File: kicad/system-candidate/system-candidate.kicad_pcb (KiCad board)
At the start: 4 copper layers, 153 x 79.1 mm, 76 parts, among them J1 691137710002 2P 5.00mm, J2 Auxiliary 12V, J3 Differential audio, J4 Control 2x4: 3V3 RESET FAULT 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, J5 691137710002 2P 5.00mm, J6 GND braid solder bond - NO mo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, U1 TPA3255DDV, U2 OPA1656ID, U3 OPA1656ID

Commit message: feat(eda): capture discrete D-020 sequencer and integrate D-021 power into system candidate
- seq-d020 (D-023): LP2985 3.3 V, two TPS3808 stages (>=360 ms hold),
  74LVC2G74 RUN/ARMED latches (human start edge with CLIP_OTW high, FAULT
  arming and latch with human re-arm), 0.62-1.44 s start timeout, TPS3700
  windows for ANALOG_12V and VMID on the RAILS_OK wired-AND.
- seq_d020_logic simulates the captured netlist; mutation-checked tests.
- system-candidate: power and seq banks outside the OEM outline, 150
  footprints, 421 native pins matched; PVDD_36V renamed PVDD; J4/R7/R8 DNP.
  ERC equal to base (4 PBTL OUT_x, 1 MONO_BIASED), DRC 0, 338 unrouted.
- power-d021: candidate stock footprints, SEQ_3V3 pull-up, manifest restored.
- 3D gallery adds system candidate views framed to show import banks.
- D-019 isolation, discharge, DC sense and mute remain NOT implemented.
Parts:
- added C301: 4700u 63V, Capacitor_THT:CP_Radial_D25.0mm_P10.00mm_SnapIn, F.Cu at (350.0, 130.0)
- added C302: 4700u 63V, Capacitor_THT:CP_Radial_D25.0mm_P10.00mm_SnapIn, F.Cu at (390.0, 130.0)
- added C310: 2.2u 100V X7R, Capacitor_SMD:C_1210_3225Metric, F.Cu at (310.0, 162.0)
- added C311: 2.2u 100V X7R, Capacitor_SMD:C_1210_3225Metric, F.Cu at (350.0, 162.0)
- added C312: 2.2n 50V X7R, Capacitor_SMD:C_0402_1005Metric, F.Cu at (390.0, 162.0)
- added C313: 3.3n, Capacitor_SMD:C_0603_1608Metric, F.Cu at (390.0, 194.0)
- added C314: 56p, Capacitor_SMD:C_0603_1608Metric, F.Cu at (190.0, 226.0)
- added C315: 22u 25V X7R, Capacitor_SMD:C_1210_3225Metric, F.Cu at (230.0, 226.0)
- added C316: 22u 25V X7R, Capacitor_SMD:C_1210_3225Metric, F.Cu at (270.0, 226.0)
- added C320: 100n, Capacitor_SMD:C_0603_1608Metric, F.Cu at (230.0, 258.0)
- added C401: 1u 25V, Capacitor_SMD:C_0603_1608Metric, F.Cu at (412.0, 25.0)
- added C402: 10n, Capacitor_SMD:C_0603_1608Metric, F.Cu at (434.0, 25.0)
- added C403: 2.2u 10V, Capacitor_SMD:C_0603_1608Metric, F.Cu at (456.0, 25.0)
- added C404: 180n, Capacitor_SMD:C_0603_1608Metric, F.Cu at (456.0, 43.0)
- added C405: 1u, Capacitor_SMD:C_0603_1608Metric, F.Cu at (390.0, 61.0)
- added C406: 100n, Capacitor_SMD:C_0603_1608Metric, F.Cu at (412.0, 79.0)
- added C407: 100n, Capacitor_SMD:C_0603_1608Metric, F.Cu at (434.0, 79.0)
- added C408: 100n, Capacitor_SMD:C_0603_1608Metric, F.Cu at (456.0, 79.0)
- added C409: 100n, Capacitor_SMD:C_0603_1608Metric, F.Cu at (478.0, 79.0)
- added C410: 100n, Capacitor_SMD:C_0603_1608Metric, F.Cu at (500.0, 79.0)
- added C411: 100n, Capacitor_SMD:C_0603_1608Metric, F.Cu at (522.0, 79.0)
- added C412: 100n, Capacitor_SMD:C_0603_1608Metric, F.Cu at (544.0, 79.0)
- added C413: 100n, Capacitor_SMD:C_0603_1608Metric, F.Cu at (390.0, 97.0)
- added C414: 100n, Capacitor_SMD:C_0603_1608Metric, F.Cu at (412.0, 97.0)
- added C415: 100n, Capacitor_SMD:C_0603_1608Metric, F.Cu at (434.0, 97.0)
- added C416: 100n, Capacitor_SMD:C_0603_1608Metric, F.Cu at (500.0, 115.0)
- added C417: 100n, Capacitor_SMD:C_0603_1608Metric, F.Cu at (522.0, 115.0)
- added D301: RECT >=400V, Diode_THT:D_P600_R-6_P12.70mm_Horizontal, F.Cu at (270.0, 130.0)
- added D302: RECT >=400V, Diode_THT:D_P600_R-6_P12.70mm_Horizontal, F.Cu at (310.0, 130.0)
- added D303: TVS VWM>=51V, Diode_SMD:D_SMC, F.Cu at (230.0, 162.0)
- added F301: T8A slow, Fuse:Fuseholder_Cylinder-5x20mm_Schurter_0031_8201_Horizontal_Open, F.Cu at (230.0, 130.0)
- added J301: T1_SECONDARY, Connector_JST:JST_VH_B3P-VH_1x03_P3.96mm_Vertical, F.Cu at (190.0, 130.0)
- added J401: START_BUTTON, Connector_PinHeader_2.54mm:PinHeader_1x02_P2.54mm_Vertical, F.Cu at (500.0, 43.0)
- added L301: 68u, Inductor_SMD:L_Coilcraft_MSS1246T-XXX, F.Cu at (190.0, 194.0)
- added R301: 4.7k 2W, Resistor_THT:R_Axial_DIN0414_L11.9mm_D4.5mm_P15.24mm_Horizontal, F.Cu at (190.0, 162.0)
- added R310: 100k 1%, Resistor_SMD:R_0603_1608Metric, F.Cu at (230.0, 194.0)
- added R311: 453k 1%, Resistor_SMD:R_0603_1608Metric, F.Cu at (270.0, 194.0)
- added R312: 49.9k 1%, Resistor_SMD:R_0603_1608Metric, F.Cu at (310.0, 194.0)
- added R313: 453k 1%, Resistor_SMD:R_0603_1608Metric, F.Cu at (350.0, 194.0)
- added R320: 931k 0.1%, Resistor_SMD:R_1206_3216Metric, F.Cu at (350.0, 226.0)
- added R321: 6.04k 0.1%, Resistor_SMD:R_0603_1608Metric, F.Cu at (390.0, 226.0)
- added R322: 7.32k 0.1%, Resistor_SMD:R_0603_1608Metric, F.Cu at (190.0, 258.0)
- added R323: 100k, Resistor_SMD:R_0603_1608Metric, F.Cu at (270.0, 258.0)
- added R401: 100k, Resistor_SMD:R_0603_1608Metric, F.Cu at (500.0, 25.0)
- added R402: 100k, Resistor_SMD:R_0603_1608Metric, F.Cu at (522.0, 25.0)
- added R403: 100k, Resistor_SMD:R_0603_1608Metric, F.Cu at (390.0, 43.0)
- added R404: 100k, Resistor_SMD:R_0603_1608Metric, F.Cu at (412.0, 43.0)
- added R405: 100k, Resistor_SMD:R_0603_1608Metric, F.Cu at (478.0, 43.0)
- added R406: 100k, Resistor_SMD:R_0603_1608Metric, F.Cu at (522.0, 43.0)
- added R407: 10k, Resistor_SMD:R_0603_1608Metric, F.Cu at (544.0, 43.0)
- added R408: 1k, Resistor_SMD:R_0603_1608Metric, F.Cu at (456.0, 61.0)
- added R420: 1M, Resistor_SMD:R_0603_1608Metric, F.Cu at (500.0, 97.0)
- added R421: 46.4k, Resistor_SMD:R_0603_1608Metric, F.Cu at (522.0, 97.0)
- added R422: 1M, Resistor_SMD:R_0603_1608Metric, F.Cu at (544.0, 97.0)
- added R423: 30.1k, Resistor_SMD:R_0603_1608Metric, F.Cu at (390.0, 115.0)
- added R424: 909k, Resistor_SMD:R_0603_1608Metric, F.Cu at (412.0, 115.0)
- added R425: 101k, Resistor_SMD:R_0603_1608Metric, F.Cu at (434.0, 115.0)
- added R426: 1M, Resistor_SMD:R_0603_1608Metric, F.Cu at (456.0, 115.0)
- added R427: 64.9k, Resistor_SMD:R_0603_1608Metric, F.Cu at (478.0, 115.0)
- added U302: LM5164DDA, Package_SO:HSOP-8-1EP_3.9x4.9mm_P1.27mm_EP2.41x3.1mm, F.Cu at (270.0, 162.0)
- added U303: TPS3700DDC, Package_TO_SOT_SMD:SOT-23-6, F.Cu at (310.0, 226.0)
- added U401: LP2985-33, Package_TO_SOT_SMD:SOT-23-5, F.Cu at (390.0, 25.0)
- added U402: TPS3808G33, Package_TO_SOT_SMD:SOT-23-6, F.Cu at (478.0, 25.0)
- added U403: TPS3808G33, Package_TO_SOT_SMD:SOT-23-6, F.Cu at (544.0, 25.0)
- added U404: TPS3808G33, Package_TO_SOT_SMD:SOT-23-6, F.Cu at (434.0, 43.0)
- added U405: 74LVC1G14, Package_TO_SOT_SMD:SOT-23-5, F.Cu at (412.0, 61.0)
- added U406: 74LVC2G74, Package_SO:SSOP-8_2.95x2.8mm_P0.65mm, F.Cu at (434.0, 61.0)
- added U407: 74LVC2G74, Package_SO:SSOP-8_2.95x2.8mm_P0.65mm, F.Cu at (478.0, 61.0)
- added U408: 74LVC1G32, Package_TO_SOT_SMD:SOT-23-5, F.Cu at (500.0, 61.0)
- added U409: 74LVC1G07, Package_TO_SOT_SMD:SOT-23-5, F.Cu at (522.0, 61.0)
- added U410: 74LVC1G08, Package_TO_SOT_SMD:SOT-23-5, F.Cu at (544.0, 61.0)
- added U411: 74LVC1G06, Package_TO_SOT_SMD:SOT-23-5, F.Cu at (390.0, 79.0)
- added U412: TPS3700DDC, Package_TO_SOT_SMD:SOT-23-6, F.Cu at (456.0, 97.0)
- added U413: TPS3700DDC, Package_TO_SOT_SMD:SOT-23-6, F.Cu at (478.0, 97.0)
- moved R104 329.6 mm to (340.0, 25.0)
- moved C101 303.3 mm to (310.0, 47.0)
- moved C102 298.8 mm to (340.0, 47.0)
- moved C106 277.8 mm to (280.0, 69.0)
- moved C107 273.4 mm to (310.0, 69.0)
- moved C108 269.0 mm to (340.0, 69.0)
- moved R202 253.3 mm to (250.0, 91.0)
- moved R203 249.1 mm to (280.0, 91.0)
- moved R204 244.9 mm to (310.0, 91.0)
- moved R205 240.7 mm to (340.0, 91.0)
- moved R207 230.2 mm to (220.0, 113.0)
- moved C201 226.2 mm to (250.0, 113.0)
- moved C202 222.2 mm to (280.0, 113.0)
- moved C203 218.3 mm to (310.0, 113.0)
- moved U2 184.5 mm to (190.0, 25.0)
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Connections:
- net /PVDD_36V renamed /PVDD

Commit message: feat(eda): complete D-019 input interface with Form C relay, mute and DC observation
- iso-d019 (D-024): Omron G6K-2F DC12 after C20/C21 (COM isolated plate,
  NO TPA pin, NC 1k discharge; break-before-make, isolated when unpowered),
  TMUX6219 mute DIVIDED->VMID, TPS3700 DC windows on both pins (2-5 V,
  tau ~50 ms) and AUX_RAW window, MMBT3904 relay/mute drivers.
- seq-d020: RESET released 12-28 ms after relay command, DC dwell 12-28 ms
  before AUDIO_EN latch, DC loss trips RAILS_OK, start timeout covers dwell.
- simulate_d019: 1350 ngspice cases, pin -0.262..6.61 V within -0.3..7 V
  (worst with pessimistic 10 ms opening; >= 0 V at datasheet 3 ms).
- system-candidate: 200 footprints, 570 pins matched, bridge closed only
  via K501, J3 DNP; ERC equal to base, DRC 0, 464 unrouted.
- Not covered: single-fault preamp rail/driver short, real TPA input when
  unpowered, contact bounce/stuck, content below 20 Hz.
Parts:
- added C418: 100n, Capacitor_SMD:C_0603_1608Metric, F.Cu at (508.0, 115.0)
- added C419: 100n, Capacitor_SMD:C_0603_1608Metric, F.Cu at (530.0, 115.0)
- added C420: 100n, Capacitor_SMD:C_0603_1608Metric, F.Cu at (552.0, 115.0)
- added C421: 100n, Capacitor_SMD:C_0603_1608Metric, F.Cu at (574.0, 115.0)
- added C422: 100n, Capacitor_SMD:C_0603_1608Metric, F.Cu at (420.0, 133.0)
- added C423: 100n, Capacitor_SMD:C_0603_1608Metric, F.Cu at (442.0, 133.0)
- added C503: 4.7n C0G, Capacitor_SMD:C_0603_1608Metric, F.Cu at (420.0, 205.0)
- added C504: 4.7n C0G, Capacitor_SMD:C_0603_1608Metric, F.Cu at (442.0, 205.0)
- added C505: 100n, Capacitor_SMD:C_0603_1608Metric, F.Cu at (574.0, 245.0)
- added C506: 100n, Capacitor_SMD:C_0603_1608Metric, F.Cu at (420.0, 265.0)
- added C507: 100n, Capacitor_SMD:C_0603_1608Metric, F.Cu at (442.0, 265.0)
- added C508: 100n, Capacitor_SMD:C_0603_1608Metric, F.Cu at (464.0, 265.0)
- added C509: 330n, Capacitor_SMD:C_0603_1608Metric, F.Cu at (464.0, 225.0)
- added C510: 680n, Capacitor_SMD:C_0603_1608Metric, F.Cu at (486.0, 225.0)
- added C511: 330n, Capacitor_SMD:C_0603_1608Metric, F.Cu at (508.0, 225.0)
- added C512: 680n, Capacitor_SMD:C_0603_1608Metric, F.Cu at (530.0, 225.0)
- added D501: 1N4148W, Diode_SMD:D_SOD-123, F.Cu at (508.0, 185.0)
- added D502: BZT52C15, Diode_SMD:D_SOD-123, F.Cu at (530.0, 185.0)
- added K501: G6K-2F DC12, Relay_SMD:Relay_DPDT_Omron_G6K-2F, F.Cu at (420.0, 185.0)
- added Q501: MMBT3904, Package_TO_SOT_SMD:SOT-23, F.Cu at (442.0, 185.0)
- added Q502: MMBT3904, Package_TO_SOT_SMD:SOT-23, F.Cu at (508.0, 245.0)
- added R428: 100k, Resistor_SMD:R_0603_1608Metric, F.Cu at (508.0, 61.0)
- added R429: 100k, Resistor_SMD:R_0603_1608Metric, F.Cu at (530.0, 97.0)
- added R430: 100k, Resistor_SMD:R_0603_1608Metric, F.Cu at (420.0, 115.0)
- added R501: 2.2k, Resistor_SMD:R_0603_1608Metric, F.Cu at (464.0, 185.0)
- added R502: 100k, Resistor_SMD:R_0603_1608Metric, F.Cu at (486.0, 185.0)
- added R503: 1k, Resistor_SMD:R_0603_1608Metric, F.Cu at (552.0, 185.0)
- added R504: 1k, Resistor_SMD:R_0603_1608Metric, F.Cu at (574.0, 185.0)
- added R505: 787k, Resistor_SMD:R_0603_1608Metric, F.Cu at (508.0, 205.0)
- added R506: 115k, Resistor_SMD:R_0603_1608Metric, F.Cu at (530.0, 205.0)
- added R507: 78.7k, Resistor_SMD:R_0603_1608Metric, F.Cu at (552.0, 205.0)
- added R508: 787k, Resistor_SMD:R_0603_1608Metric, F.Cu at (574.0, 205.0)
- added R509: 115k, Resistor_SMD:R_0603_1608Metric, F.Cu at (420.0, 225.0)
- added R510: 78.7k, Resistor_SMD:R_0603_1608Metric, F.Cu at (442.0, 225.0)
- added R511: 100k, Resistor_SMD:R_0603_1608Metric, F.Cu at (486.0, 245.0)
- added R512: 10k, Resistor_SMD:R_0603_1608Metric, F.Cu at (530.0, 245.0)
- added R513: 100k, Resistor_SMD:R_0603_1608Metric, F.Cu at (552.0, 245.0)
- added R514: 357k, Resistor_SMD:R_0603_1608Metric, F.Cu at (574.0, 225.0)
- added R515: 1.5k, Resistor_SMD:R_0603_1608Metric, F.Cu at (420.0, 245.0)
- added R516: 11.5k, Resistor_SMD:R_0603_1608Metric, F.Cu at (442.0, 245.0)
- added U414: TPS3808G33, Package_TO_SOT_SMD:SOT-23-6, F.Cu at (486.0, 61.0)
- added U415: 74LVC1G08, Package_TO_SOT_SMD:SOT-23-5, F.Cu at (552.0, 97.0)
- added U416: TPS3808G33, Package_TO_SOT_SMD:SOT-23-6, F.Cu at (574.0, 97.0)
- added U417: 74LVC2G74, Package_SO:SSOP-8_2.95x2.8mm_P0.65mm, F.Cu at (442.0, 115.0)
- added U418: 74LVC1G32, Package_TO_SOT_SMD:SOT-23-5, F.Cu at (464.0, 115.0)
- added U419: 74LVC1G07, Package_TO_SOT_SMD:SOT-23-5, F.Cu at (486.0, 115.0)
- added U501: TPS3700DDC, Package_TO_SOT_SMD:SOT-23-6, F.Cu at (464.0, 205.0)
- added U502: TPS3700DDC, Package_TO_SOT_SMD:SOT-23-6, F.Cu at (486.0, 205.0)
- added U503: TMUX6219, Package_SO:MSOP-8_3x3mm_P0.65mm, F.Cu at (464.0, 245.0)
- added U504: TPS3700DDC, Package_TO_SOT_SMD:SOT-23-6, F.Cu at (552.0, 225.0)
- moved R423 184.9 mm to (574.0, 133.0)
- moved C411 103.6 mm to (420.0, 97.0)
- moved C412 103.6 mm to (442.0, 97.0)
- moved U409 103.6 mm to (420.0, 79.0)
- moved U410 103.6 mm to (442.0, 79.0)
- moved C406 74.0 mm to (486.0, 79.0)
- moved C407 74.0 mm to (508.0, 79.0)
- moved C408 74.0 mm to (530.0, 79.0)
- moved C409 74.0 mm to (552.0, 79.0)
- moved C410 74.0 mm to (574.0, 79.0)
- moved C413 74.0 mm to (464.0, 97.0)
- moved C414 74.0 mm to (486.0, 97.0)
- moved C415 74.0 mm to (508.0, 97.0)
- moved R408 74.0 mm to (530.0, 61.0)
- moved U407 74.0 mm to (552.0, 61.0)
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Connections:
- C104 pad 2: /DIFF_POS -> /DIFF_P
- C105 pad 2: /DIFF_POS -> /DIFF_P
- C20 pad 2: /INPUT_A_AC -> /INA_ISO
- C21 pad 2: /INPUT_B_AC -> /INB_ISO
- R107 pad 1: /DIFF_POS -> /DIFF_P
- R108 pad 1: /DIFF_NEG -> /DIFF_N
- R408 pad 1: /RUN -> /RESET_GO
- U3 pad 1: /DIFF_POS -> /DIFF_P
- U3 pad 2: /DIFF_POS -> /DIFF_P
- U3 pad 7: /DIFF_NEG -> /DIFF_N
- U407 pad 5: unconnected-(U407-Q-Pad5) -> /ARMED
- U410 pad 2: /NOT_ARMED -> /NOT_AUDIO

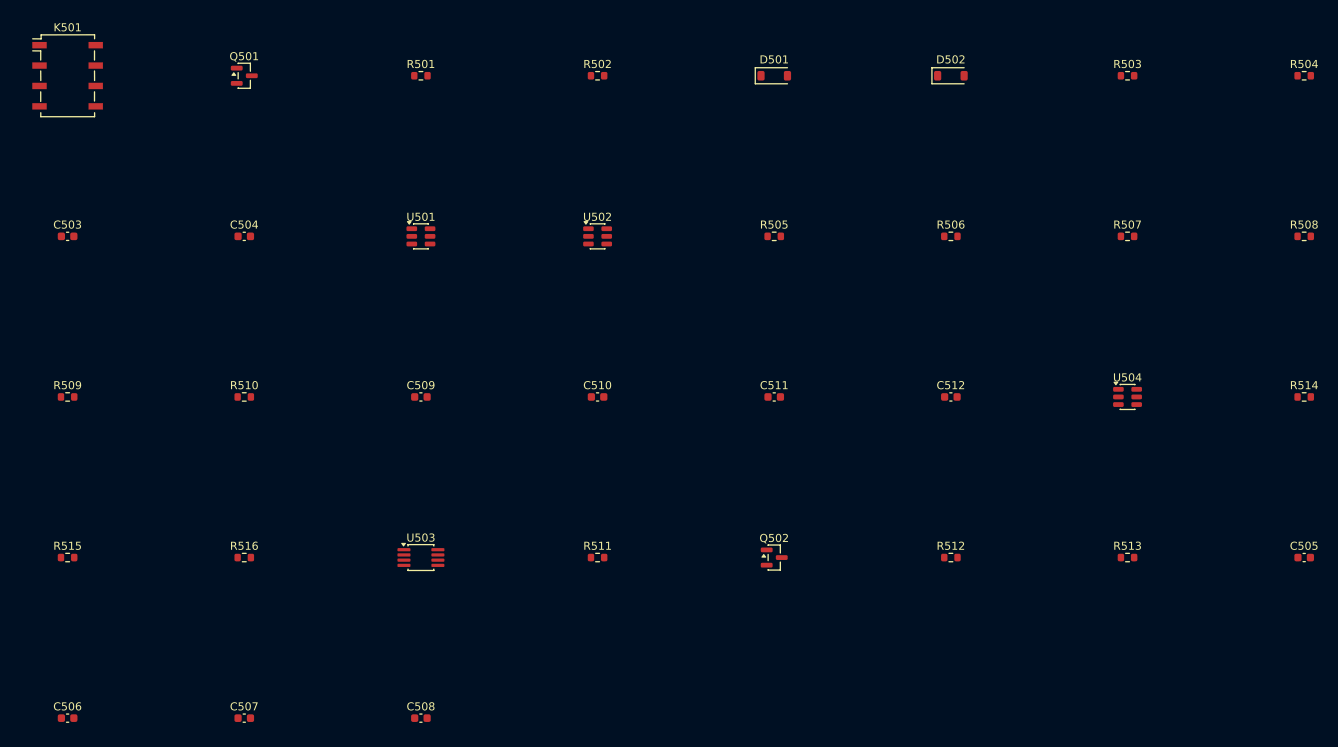
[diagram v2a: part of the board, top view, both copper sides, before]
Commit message: feat(eda): clamp TPA inputs against single faults and audit TMUX6219 land pattern
- D-024a: 3.3k series after relay NO plus BAT54 (K on pin, A to GND).
  Driver shorted low with relay closed: about -5.9 V unclamped, <= -0.351 V
  at datasheet maximum VF (still 51 mV beyond -0.3 V); gain -1.33 dB typ.
- simulate_d019: 216 single-fault cases; normal cases now -0.158..6.47 V.
- Local TI DGK0008A footprint (SCDS420E p.50) replaces generic MSOP-8.
- Risk table in iso-d019.md: bounce resolved by design, sub-20 Hz fails
  safe, stuck-high driver and unpowered TPA input remain open.
- system-candidate: 204 footprints, 580 pins matched, DRC 0; gallery and
  SVG regenerated.
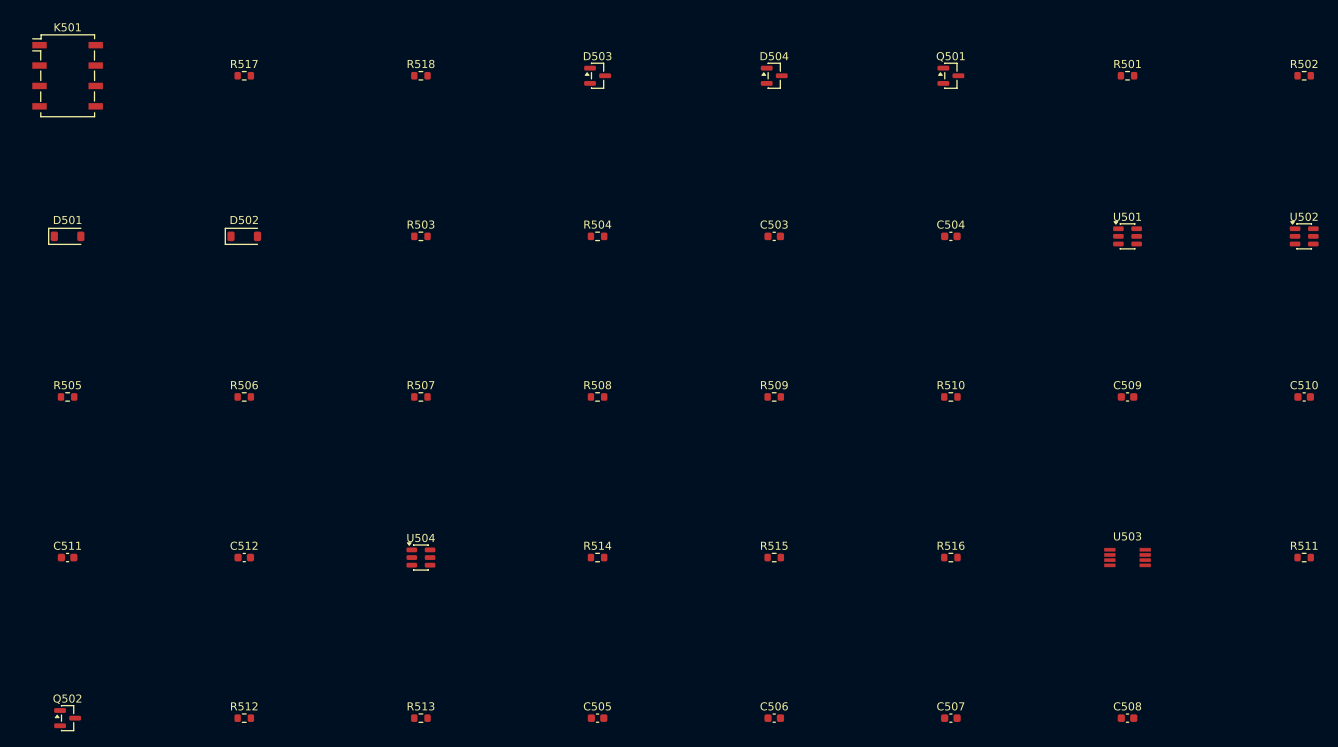
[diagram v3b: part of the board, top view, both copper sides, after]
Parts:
- added D503: BAT54, Package_TO_SOT_SMD:SOT-23, F.Cu at (486.0, 185.0)
- added D504: BAT54, Package_TO_SOT_SMD:SOT-23, F.Cu at (508.0, 185.0)
- added R517: 3.3k, Resistor_SMD:R_0603_1608Metric, F.Cu at (442.0, 185.0)
- added R518: 3.3k, Resistor_SMD:R_0603_1608Metric, F.Cu at (464.0, 185.0)
- U503: footprint Package_SO:MSOP-8_3x3mm_P0.65mm -> PS28_ANALOG:TI_DGK0008A
- moved C505 90.2 mm to (486.0, 265.0)
- moved C511 90.2 mm to (420.0, 245.0)
- moved C512 90.2 mm to (442.0, 245.0)
- moved D501 90.2 mm to (420.0, 205.0)
- moved D502 90.2 mm to (442.0, 205.0)
- moved Q502 90.2 mm to (420.0, 265.0)
- moved R503 90.2 mm to (464.0, 205.0)
- moved R504 90.2 mm to (486.0, 205.0)
- moved R505 90.2 mm to (420.0, 225.0)
- moved R506 90.2 mm to (442.0, 225.0)
- moved R507 90.2 mm to (464.0, 225.0)
- moved R508 90.2 mm to (486.0, 225.0)
- moved R512 90.2 mm to (442.0, 265.0)
- moved R513 90.2 mm to (464.0, 265.0)
- moved R514 90.2 mm to (486.0, 245.0)
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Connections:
- K501 pad 4: /INPUT_A_AC -> /INA_NO
- K501 pad 5: /INPUT_B_AC -> /INB_NO
